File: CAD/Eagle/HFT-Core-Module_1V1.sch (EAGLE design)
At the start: 399 parts, among them Q0521 ABS07-32.768KHZ, Q0811 ABM03B-32.000MHZ, Q0911 ABM3B-16MHZ-10-R50-1-U, T1201 MMBT2222, T1202 MMBT2222, T1203 MMBT2222, U0111 STM32L4Z_144PIN_SMPS, U0431 PAM2305AAB120, U0601 LM4120IM5-3.0, U0611 MAX5217, U0631 CFPT-141-20MHZ, U0641 OPA354, U0701 Si5338, U0801 SX1276, U0901 AX5243, U0911 PE4259, U0921 PE4259, U0991 PE4259, U1101 MCP3911A0-E-SS, U1111 MAX5136AGTG+, U1121 OPA354, U1131 OPA354, U1141 OPA354, U1201 NHD-C0220BIZ_2X20CHARS, U1301 MPU-9250, U1311 MS5607-02BA03, U1321 SHT31-DIS, U1401 SOLARPANEL_3V3_5MA1_25MM_X_20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, U1402 SPV1040T, U1501 TS5A23166, U1601 SC189ZSKTRT, U1701 TS5A23166, U1801 TS5A23166, U1901 TS5A23166, X1261 TTE_EN11-HSM, X2001 MOLEX 105017-0001, X2101 SMA_SMT_AMPHENOL-901-143, SAM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, X2111 SMA_SMT_AMPHENOL-901-143, SAM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, X2201 CUI SJ1-3535NS, X2211 CUI SJ1-3535NS, X2311 2X20/90_1MM27_HARWIN_M50-3202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, X2312 2X20/90_1MM27_HARWIN_M50-3202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, X2321 2X20/90_1MM27_HARWIN_M50-3202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, X2322 2X20/90_1MM27_HARWIN_M50-3202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, X2331 2X20/90_1MM27_HARWIN_M50-3202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, X2332 2X20/90_1MM27_HARWIN_M50-3202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

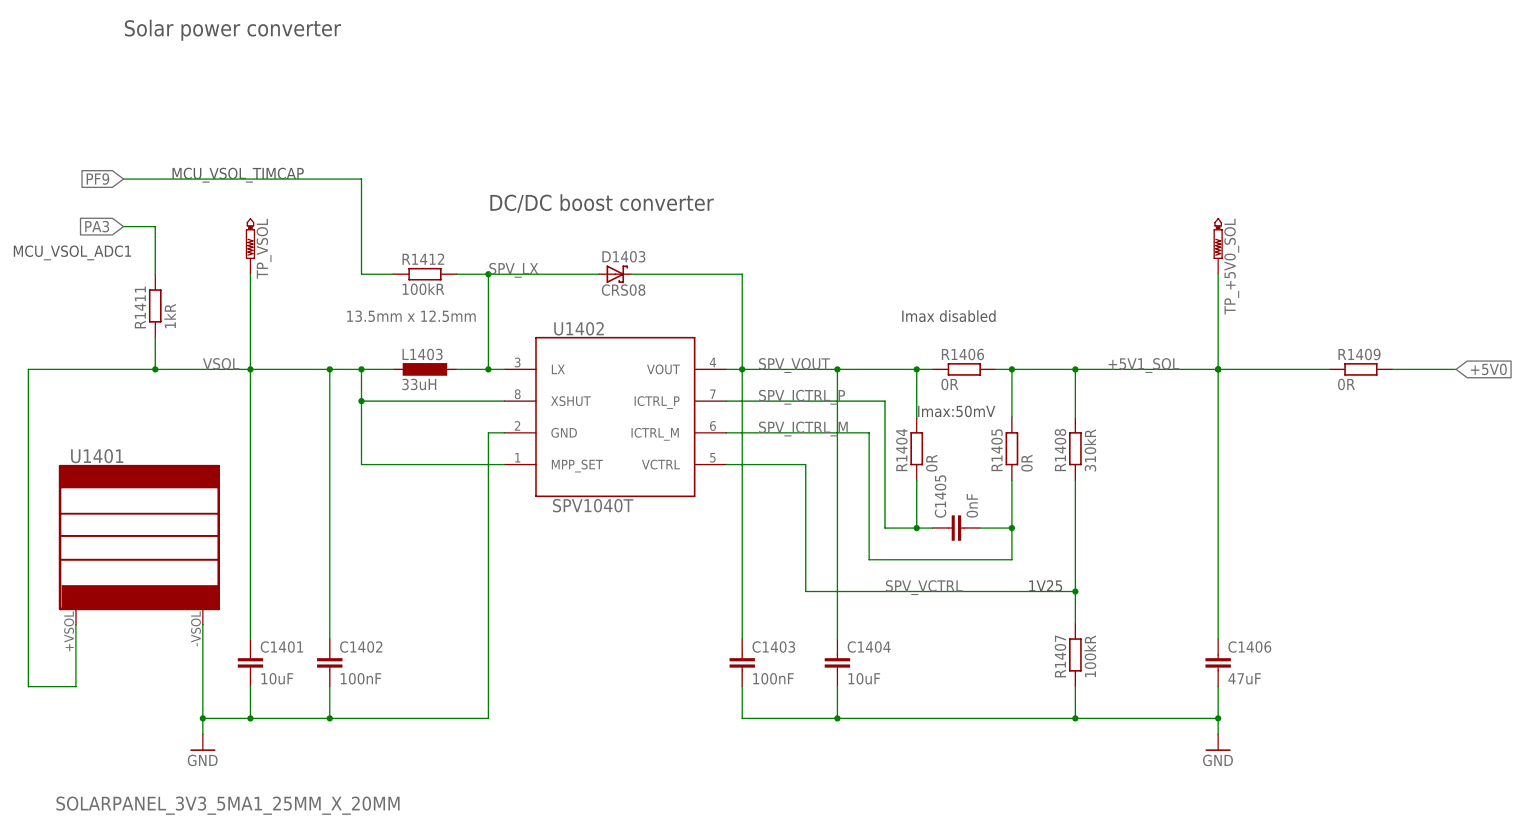
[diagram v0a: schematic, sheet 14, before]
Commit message: HW_1V1 - CAD/Eagle - New 1F capacitor C115_080x160_POL added
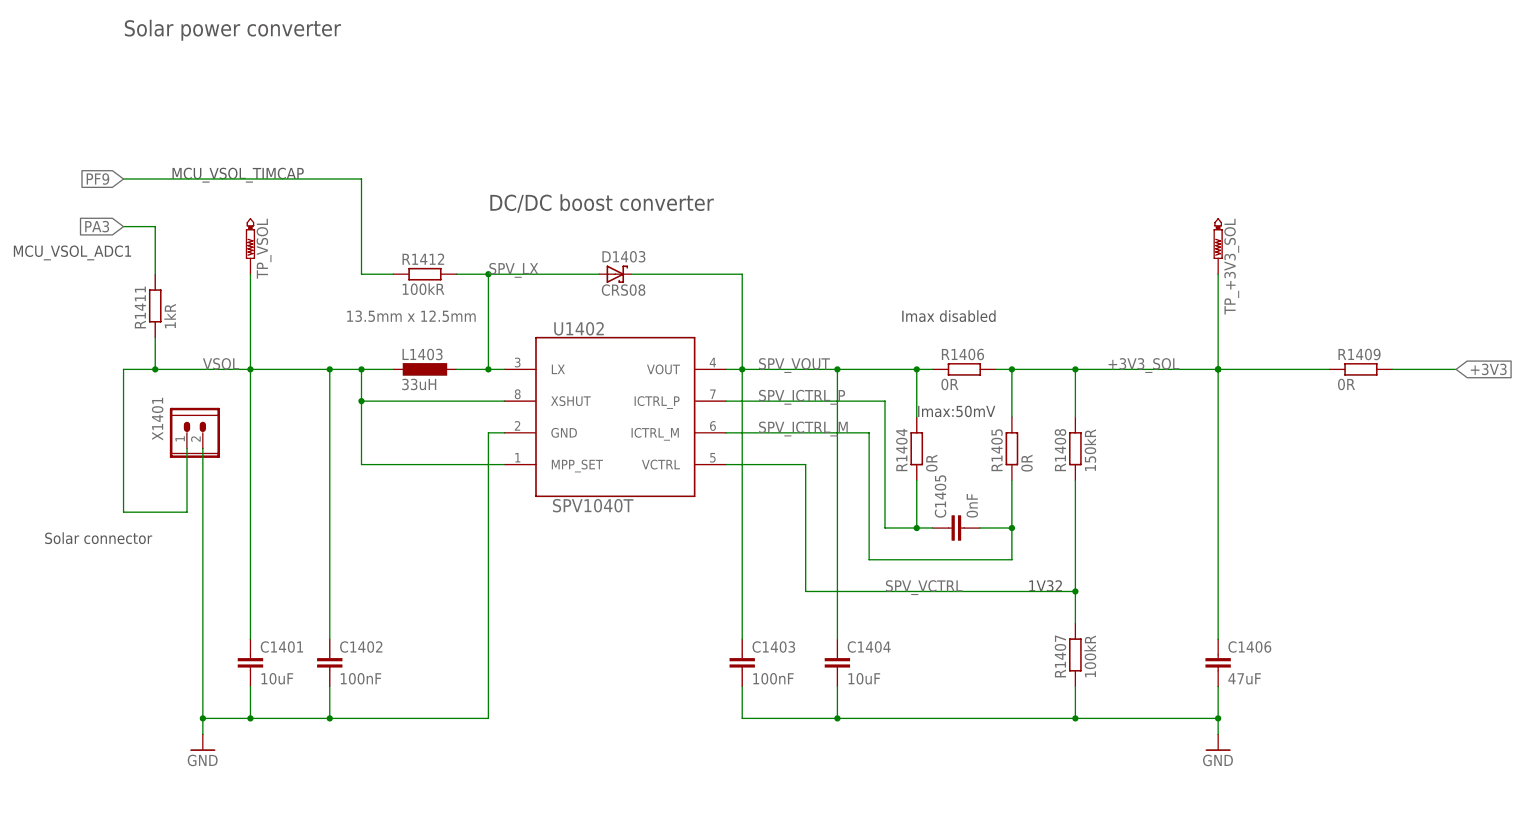
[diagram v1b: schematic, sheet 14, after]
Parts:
- removed C1601: 1F_EEC-S5R5H105N, df4iah_rcl:CPOL-EUW14MM_D8MM_P13MM5
- removed U1401: SOLARPANEL_3V3_5MA1_25MM_X_20MM, df4iah_supply:SOLARPANEL_3V3_5MA1_25MM_X_20MM
- added X1401: WIRE-TO-BOARD_5MM08_1X02, df4iah_connector:WIRE-TO-BOARD_5MM08_1X02
- C0451, C1607: device df4iah_rcl:CPOL-EUW14MM_D8MM_P13MM5 -> df4iah_rcl:CPOL-EUC115-080X160_POL
- R1408: value 310kR -> 150kR
- renumbered TP_+5V0_SOL to TP_+3V3_SOL
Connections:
- net +5V1_SOL renamed +3V3_SOL
- net +3V3: now also R1409.2
- net +5V0: no longer C1601.+, R1409.2
- net GND: now also X1401.2; no longer C1601.-, U1401.-VSOL
- net VSOL: now also X1401.1; no longer U1401.+VSOL
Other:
- note added: "1V32"
- note added: "Solar connector"
- note removed: "1V25"
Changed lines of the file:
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@@
 <part name="C0441" library="rcl" deviceset="C-EU" device="C0603" value="100nF"/>
 <part name="D0451" library="df4iah_diode" deviceset="D_SOD923" device="" value="CMAD6001"/>
-<part name="C0451" library="df4iah_rcl" deviceset="CPOL-EU" device="W14MM_D8MM_P13MM5" value="1F_EEC-S5R5H105N"/>
+<part name="C0451" library="df4iah_rcl" deviceset="CPOL-EU" device="C115-080X160_POL" value="1F_EEC-S5R5H105N"/>
 <part name="GND0451" library="df4iah_supply" deviceset="GND" device=""/>
 <part name="C1406" library="rcl" deviceset="C-EU" device="C0805" value="47uF"/>
 <part name="GND1402" library="df4iah_supply" deviceset="GND" device=""/>
 <part name="TP_VSOL" library="testpad" deviceset="PTR1" device="B1,27" value="PTR1B1,27"/>
-<part name="TP_+5V0_SOL" library="testpad" deviceset="PTR1" device="B1,27" value="PTR1B1,27"/>
+<part name="TP_+3V3_SOL" library="testpad" deviceset="PTR1" device="B1,27" value="PTR1B1,27"/>
 <part name="FRAME_15" library="df4iah_frame" deviceset="A4L-LOC" device="" value="I2C connector"/>
 <part name="D1501" library="df4iah_diode" deviceset="CRS08" device=""/>
@@
 <part name="C1701" library="rcl" deviceset="C-EU" device="C0603" value="100nF"/>
 <part name="C1703" library="rcl" deviceset="C-EU" device="C0603" value="100nF"/>
-<part name="C1601" library="df4iah_rcl" deviceset="CPOL-EU" device="W14MM_D8MM_P13MM5" value="1F_EEC-S5R5H105N"/>
 <part name="GND1601" library="df4iah_supply" deviceset="GND" device=""/>
 <part name="TP_+5V0" library="testpad" deviceset="PTR1" device="B1,27" value="PTR1B1,27"/>
 <part name="TP_+5V0_USB_SW" library="testpad" deviceset="PTR1" device="B1,27" value="PTR1B1,27"/>
-<part name="C1607" library="df4iah_rcl" deviceset="CPOL-EU" device="W14MM_D8MM_P13MM5" value="1F_EEC-S5R5H105N"/>
+<part name="C1607" library="df4iah_rcl" deviceset="CPOL-EU" device="C115-080X160_POL" value="1F_EEC-S5R5H105N"/>
 <part name="GND1602" library="df4iah_supply" deviceset="GND" device=""/>
 <part name="X2001" library="df4iah_connector" deviceset="USB_MICRO-B_MOLEX" device="" value="MOLEX 105017-0001"/>
@@
 <part name="R1405" library="rcl" deviceset="R-EU_" device="R0603" value="0R"/>
 <part name="C1405" library="rcl" deviceset="C-EU" device="C0603" value="0nF"/>
-<part name="R1408" library="rcl" deviceset="R-EU_" device="R0603" value="310kR"/>
+<part name="R1408" library="rcl" deviceset="R-EU_" device="R0603" value="150kR"/>
 <part name="R1407" library="rcl" deviceset="R-EU_" device="R0603" value="100kR"/>
 <part name="SJ0421" library="df4iah_jumper" deviceset="SJ" device=""/>
@@
 <part name="U0611" library="df4iah_dac" deviceset="MAX5217" device=""/>
 <part name="TP_+3V3" library="testpad" deviceset="PTR1" device="B1,27" value="PTR1B1,27"/>
-<part name="U1401" library="df4iah_supply" deviceset="SOLARPANEL_3V3_5MA1_25MM_X_20MM" device=""/>
 <part name="U1201" library="df4iah_lcd" deviceset="NHD-C0220BIZ_2X20CHARS" device=""/>
 <part name="PF2011" library="rcl" deviceset="R-EU_" device="M1206" value="1.1A/2.2A"/>
@@
 <part name="R1411" library="rcl" deviceset="R-EU_" device="R0603" value="1kR"/>
 <part name="R1412" library="rcl" deviceset="R-EU_" device="R0603" value="100kR"/>
+<part name="X1401" library="df4iah_connector" deviceset="WIRE-TO-BOARD_5MM08_1X02" device=""/>
 </parts>
 <sheets>
@@
 <description>Power Solar</description>
 <plain>
-<text x="167.64" y="73.66" size="1.778" layer="97">1V25</text>
+<text x="167.64" y="73.66" size="1.778" layer="97">1V32</text>
 <text x="149.86" y="101.6" size="1.778" layer="97">Imax:50mV</text>
 <text x="58.42" y="116.84" size="1.778" layer="96">13.5mm x 12.5mm</text>
@@
 <text x="5.08" y="127.254" size="1.778" layer="97">MCU_VSOL_ADC1</text>
 <text x="30.48" y="139.7" size="1.778" layer="97">MCU_VSOL_TIMCAP</text>
+<text x="10.16" y="81.28" size="1.778" layer="97">Solar connector</text>
 </plain>
 <instances>
@@
 <instance part="GND1402" gate="1" x="198.12" y="48.26"/>
 <instance part="TP_VSOL" gate="G$1" x="43.18" y="127" rot="R180"/>
-<instance part="TP_+5V0_SOL" gate="G$1" x="198.12" y="127" rot="R180"/>
+<instance part="TP_+3V3_SOL" gate="G$1" x="198.12" y="127" rot="R180"/>
 <instance part="R1409" gate="G$1" x="220.98" y="109.22"/>
 <instance part="D1403" gate="G$1" x="101.6" y="124.46"/>
@@
 <instance part="GND1401" gate="1" x="35.56" y="48.26"/>
 <instance part="U1402" gate="G$1" x="101.6" y="101.6"/>
-<instance part="U1401" gate="G$1" x="25.4" y="81.28" smashed="yes" rot="R270">
-<attribute name="NAME" x="14.224" y="94.234" size="2.1844" layer="95" ratio="10"/>
-<attribute name="VALUE" x="11.938" y="38.608" size="2.1844" layer="96" ratio="12"/>
-</instance>
 <instance part="R1411" gate="G$1" x="27.94" y="119.38" rot="R90"/>
 <instance part="R1412" gate="G$1" x="71.12" y="124.46"/>
+<instance part="X1401" gate="G$1" x="33.02" y="99.06" rot="R90"/>
 </instances>
 <busses>
@@
 <pinref part="GND1401" gate="1" pin="GND"/>
 <pinref part="U1402" gate="G$1" pin="GND"/>
-<wire x1="35.56" y1="68.326" x2="35.56" y2="53.34" width="0.1524" layer="91"/>
+<wire x1="35.56" y1="96.52" x2="35.56" y2="53.34" width="0.1524" layer="91"/>
 <wire x1="35.56" y1="53.34" x2="35.56" y2="50.8" width="0.1524" layer="91"/>
 <wire x1="83.82" y1="99.06" x2="81.28" y2="99.06" width="0.1524" layer="91"/>
@@
 <junction x="43.18" y="53.34"/>
 <junction x="35.56" y="53.34"/>
-<pinref part="U1401" gate="G$1" pin="-VSOL"/>
+<pinref part="X1401" gate="G$1" pin="2"/>
 </segment>
 </net>
-<net name="+5V1_SOL" class="0">
+<net name="+3V3_SOL" class="0">
 <segment>
 <wire x1="162.56" y1="109.22" x2="165.1" y2="109.22" width="0.1524" layer="91"/>
 <label x="180.34" y="109.22" size="1.778" layer="95"/>
-<pinref part="TP_+5V0_SOL" gate="G$1" pin="TP"/>
+<pinref part="TP_+3V3_SOL" gate="G$1" pin="TP"/>
 <wire x1="165.1" y1="109.22" x2="175.26" y2="109.22" width="0.1524" layer="91"/>
 <wire x1="175.26" y1="109.22" x2="198.12" y2="109.22" width="0.1524" layer="91"/>
@@
 <wire x1="60.96" y1="109.22" x2="66.04" y2="109.22" width="0.1524" layer="91"/>
 <wire x1="43.18" y1="109.22" x2="27.94" y2="109.22" width="0.1524" layer="91"/>
-<wire x1="27.94" y1="109.22" x2="7.62" y2="109.22" width="0.1524" layer="91"/>
-<wire x1="7.62" y1="109.22" x2="7.62" y2="58.42" width="0.1524" layer="91"/>
-<wire x1="7.62" y1="58.42" x2="15.24" y2="58.42" width="0.1524" layer="91"/>
-<wire x1="15.24" y1="58.42" x2="15.24" y2="68.326" width="0.1524" layer="91"/>
-<pinref part="U1401" gate="G$1" pin="+VSOL"/>
+<wire x1="27.94" y1="109.22" x2="22.86" y2="109.22" width="0.1524" layer="91"/>
+<wire x1="22.86" y1="109.22" x2="22.86" y2="86.36" width="0.1524" layer="91"/>
 <pinref part="R1411" gate="G$1" pin="1"/>
 <wire x1="27.94" y1="109.22" x2="27.94" y2="114.3" width="0.1524" layer="91"/>
 <junction x="27.94" y="109.22"/>
-</segment>
-</net>
-<net name="+5V0" class="4">
-<segment>
-<wire x1="236.22" y1="109.22" x2="226.06" y2="109.22" width="0.1524" layer="91"/>
-<label x="236.22" y="109.22" size="1.778" layer="95" xref="yes"/>
-<pinref part="R1409" gate="G$1" pin="2"/>
+<wire x1="22.86" y1="86.36" x2="33.02" y2="86.36" width="0.1524" layer="91"/>
+<pinref part="X1401" gate="G$1" pin="1"/>
+<wire x1="33.02" y1="86.36" x2="33.02" y2="96.52" width="0.1524" layer="91"/>
 </segment>
 </net>
@@
 </segment>
 </net>
+<net name="+3V3" class="0">
+<segment>
+<wire x1="236.22" y1="109.22" x2="226.06" y2="109.22" width="0.1524" layer="91"/>
+<label x="236.22" y="109.22" size="1.778" layer="95" xref="yes"/>
+<pinref part="R1409" gate="G$1" pin="2"/>
+</segment>
+</net>
 </nets>
 </sheet>
@@
 <instance part="C1606" gate="G$1" x="180.34" y="76.2"/>
 <instance part="FRAME_16" gate="G$1" x="0" y="0"/>
-<instance part="C1601" gate="G$1" x="43.18" y="78.74"/>
 <instance part="GND1601" gate="1" x="43.18" y="60.96"/>
 <instance part="TP_+5V0" gate="G$1" x="73.66" y="111.76" rot="R180"/>
@@
 <segment>
 <pinref part="GND1601" gate="1" pin="GND"/>
-<pinref part="C1601" gate="G$1" pin="-"/>
 <wire x1="43.18" y1="63.5" x2="43.18" y2="66.04" width="0.1524" layer="91"/>
-<wire x1="43.18" y1="66.04" x2="43.18" y2="73.66" width="0.1524" layer="91"/>
 <wire x1="93.98" y1="66.04" x2="93.98" y2="91.44" width="0.1524" layer="91"/>
 <pinref part="U1601" gate="G$1" pin="GND"/>
 <wire x1="93.98" y1="91.44" x2="96.52" y2="91.44" width="0.1524" layer="91"/>
 <wire x1="43.18" y1="66.04" x2="73.66" y2="66.04" width="0.1524" layer="91"/>
-<junction x="43.18" y="66.04"/>
 <pinref part="C1602" gate="G$1" pin="2"/>
 <wire x1="73.66" y1="66.04" x2="93.98" y2="66.04" width="0.1524" layer="91"/>
@@
 <net name="+5V0" class="4">
 <segment>
-<wire x1="43.18" y1="116.84" x2="35.56" y2="116.84" width="0.1524" layer="91"/>
-<label x="35.56" y="116.84" size="1.778" layer="95" rot="R180" xref="yes"/>
+<label x="43.18" y="96.52" size="1.778" layer="95" rot="R180" xref="yes"/>
 <junction x="73.66" y="96.52"/>
 <wire x1="96.52" y1="96.52" x2="73.66" y2="96.52" width="0.1524" layer="91"/>
-<wire x1="43.18" y1="96.52" x2="43.18" y2="116.84" width="0.1524" layer="91"/>
-<pinref part="C1601" gate="G$1" pin="+"/>
 <pinref part="TP_+5V0" gate="G$1" pin="TP"/>
-<wire x1="43.18" y1="81.28" x2="43.18" y2="96.52" width="0.1524" layer="91"/>
 <wire x1="43.18" y1="96.52" x2="73.66" y2="96.52" width="0.1524" layer="91"/>
 <junction x="73.66" y="96.52"/>
 <wire x1="73.66" y1="96.52" x2="73.66" y2="109.22" width="0.1524" layer="91"/>
-<junction x="43.18" y="96.52"/>
 <pinref part="C1602" gate="G$1" pin="1"/>
 <wire x1="73.66" y1="96.52" x2="73.66" y2="86.36" width="0.1524" layer="91"/>
